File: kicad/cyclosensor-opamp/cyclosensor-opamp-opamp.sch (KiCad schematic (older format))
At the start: 18 parts, among them J1 RJ14, U1 TCRT5000, U2 MCP6001U, U3 MCP6001U

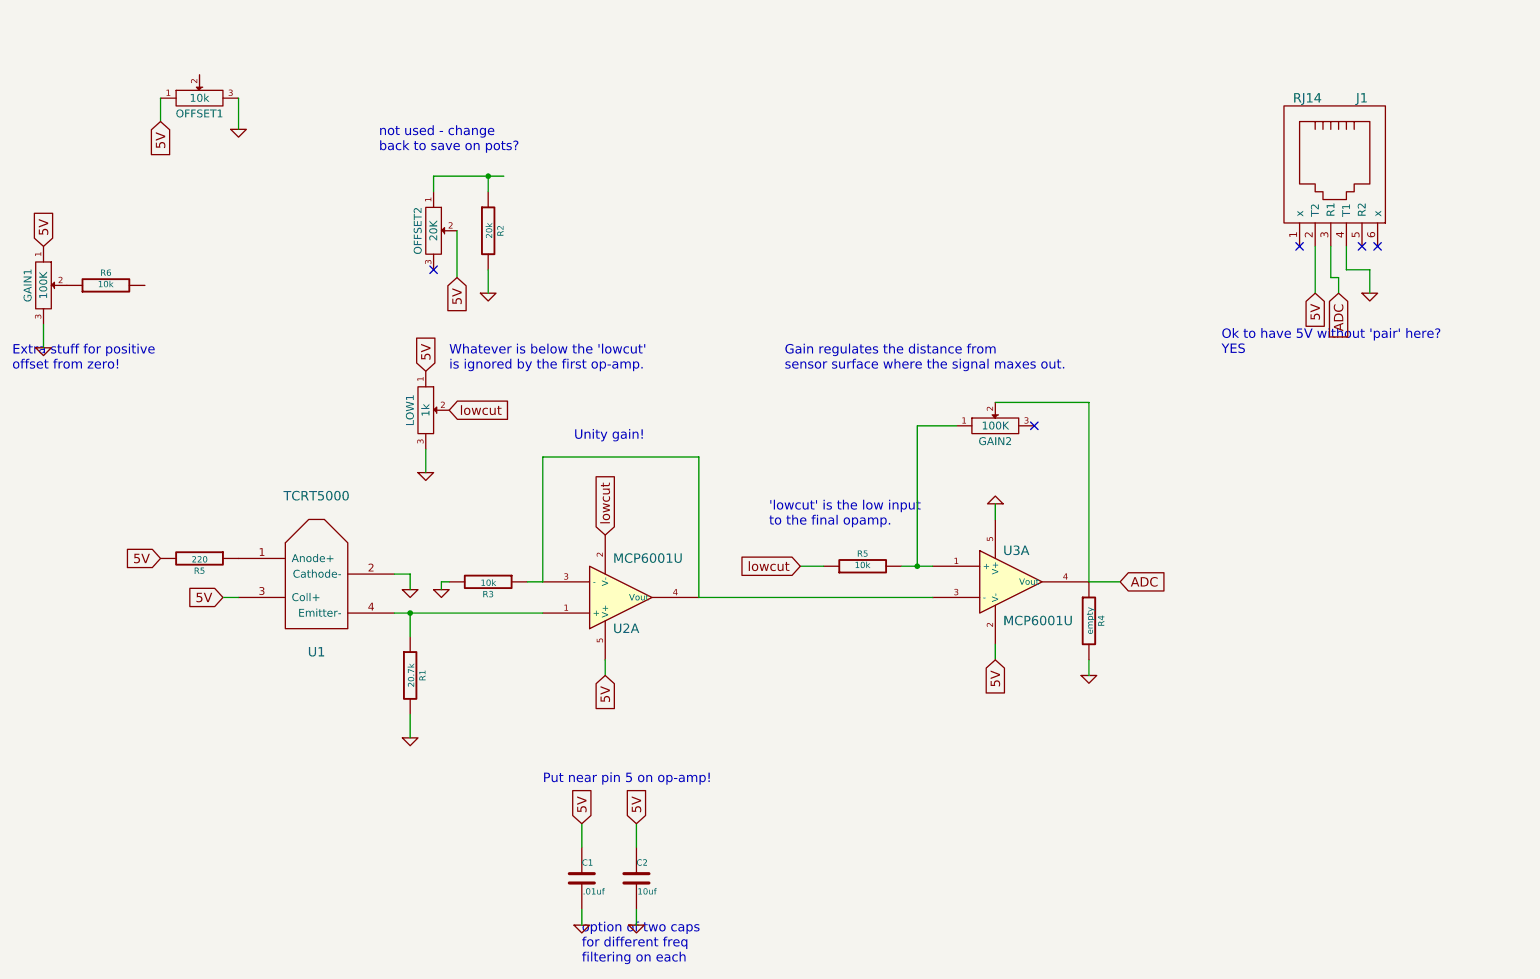
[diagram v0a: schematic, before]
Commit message: tweaks to the opamp-opamp circuit.  remove extra unused stuff.  about ready to move to the layout stage.
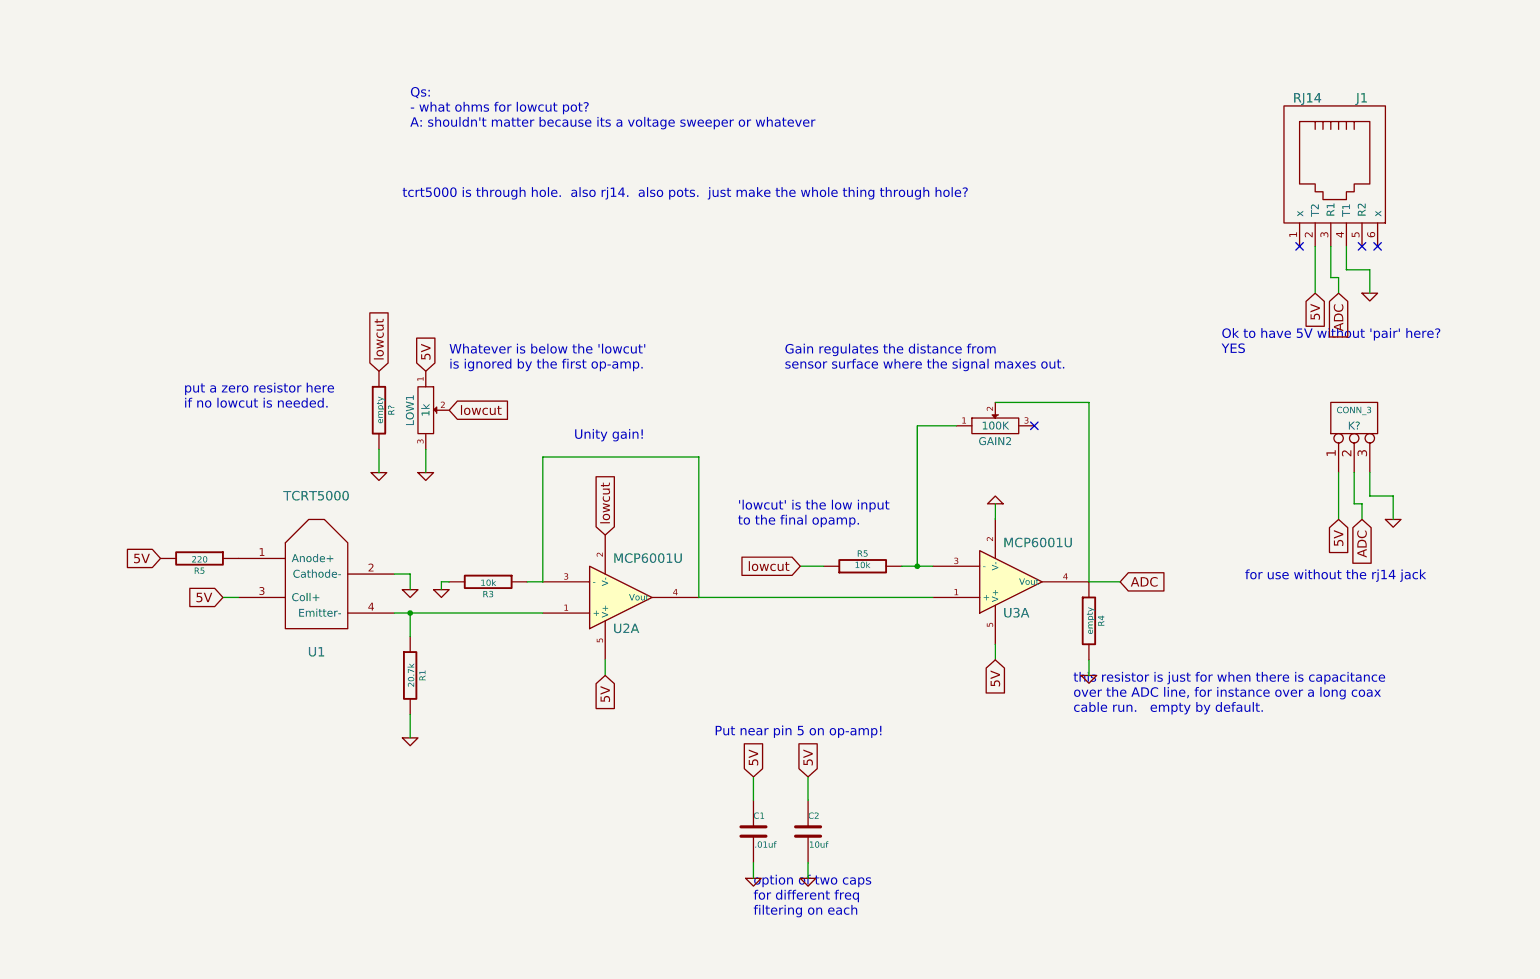
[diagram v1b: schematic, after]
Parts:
- removed GAIN1: 100K, ~, symbol POT
- removed OFFSET1: 10k, ~, symbol POT
- removed OFFSET2: 20K, ~, symbol POT
- removed R2: 20k, ~, symbol R
- removed R6: 10k, ~, symbol R
- added K?: CONN_3, symbol CONN_3
- added R?: empty, ~, symbol R
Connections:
- net 5V: now also U3.5 (V+), K?.1 (P1); no longer U3.2 (V-)
- net ADC: now also K?.2 (PM)
- net GND: now also U3.2 (V-), K?.3 (P3), R?.2; no longer U3.5 (V+)
- net lowcut: now also R?.1
- net at R3.1, U2.3 (-), U2.4 (Vout): now also U3.1 (+); no longer U3.3 (-)
- net at GAIN2.1, R5.2: now also U3.3 (-); no longer U3.1 (+)
- no-connect marks 5 -> 4
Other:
- note added: "Qs:\n- what ohms for lowcut pot?\nA: shouldn't matter because its a voltage sweeper or whatever"
- note added: "for use without the rj14 jack"
- note added: "put a zero resistor here \nif no lowcut is needed."
- note added: "tcrt5000 is through hole. also rj14. also pots. just make the whole thing through hole?"
- note added: "this resistor is just for when there is capacitance \nover the ADC line, for instance over a long coax \ncable run. empty by default."
- note removed: "Extra stuff for positive\noffset from zero!"
- note removed: "not used - change\nback to save on pots?"
- moved on the sheet: C1, C2

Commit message: big progress!  got footprints for all components, got layout started.
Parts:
- added R7, R8, R9: empty, ~, symbol R
- LOW1: value 1k -> 100k
- U1: footprint ~ -> (none)
- gave numbers to parts that had none: 2
- renumbered R5 to R1, R1 to R2, R5 to R4, R4 to R5
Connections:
- net 5V: now also R7.2
- net ADC: now also R9.2
- net lowcut: now also R7.1
- net at R2.1, U1.4 (Emitter-), U2.1 (+): now also R8.2
- net at R3.1, U2.3 (-), U2.4 (Vout)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: now also R8.1
- net at GAIN2.1, R4.2, U3.3 (-): now also R9.1
- no-connect marks 4 -> 6
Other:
- note added: "Gain regulates the distance from \nsensor surface where the signal maxes out.\nCan use a fixed resistor instead \nof the pot if desired."
- note added: "If fixed lowcut is desired, \nuse appropriate resistors here."
- note added: "Mount POTs, RJ14 on bottom of board!!"
- note added: "Q: 'lowcut' beyond op-amp specs? might blow it up?\nA: no, but its not 'correct'!"
- note added: "Qs:\n- what ohms for lowcut pot?\nA: it affects current draw. 1k to 10k for more current."
- note added: "bypass, for leaving \nout op-amp #1"
- note added: "tcrt5000 is through hole. also rj14. also pots. \njust make the whole thing through hole?"
- note removed: "Gain regulates the distance from \nsensor surface where the signal maxes out."
- note removed: "Qs:\n- what ohms for lowcut pot?\nA: shouldn't matter because its a voltage sweeper or whatever"
- note removed: "put a zero resistor here \nif no lowcut is needed."
- note removed: "tcrt5000 is through hole. also rj14. also pots. just make the whole thing through hole?"
- moved on the sheet: C1, C2, K1, R6
